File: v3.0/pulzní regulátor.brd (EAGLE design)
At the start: 27.9 x 53 mm, 18 parts, among them Q1 NX3008, Q2 NX3008, Q3 NX3008, Q4 NX3008

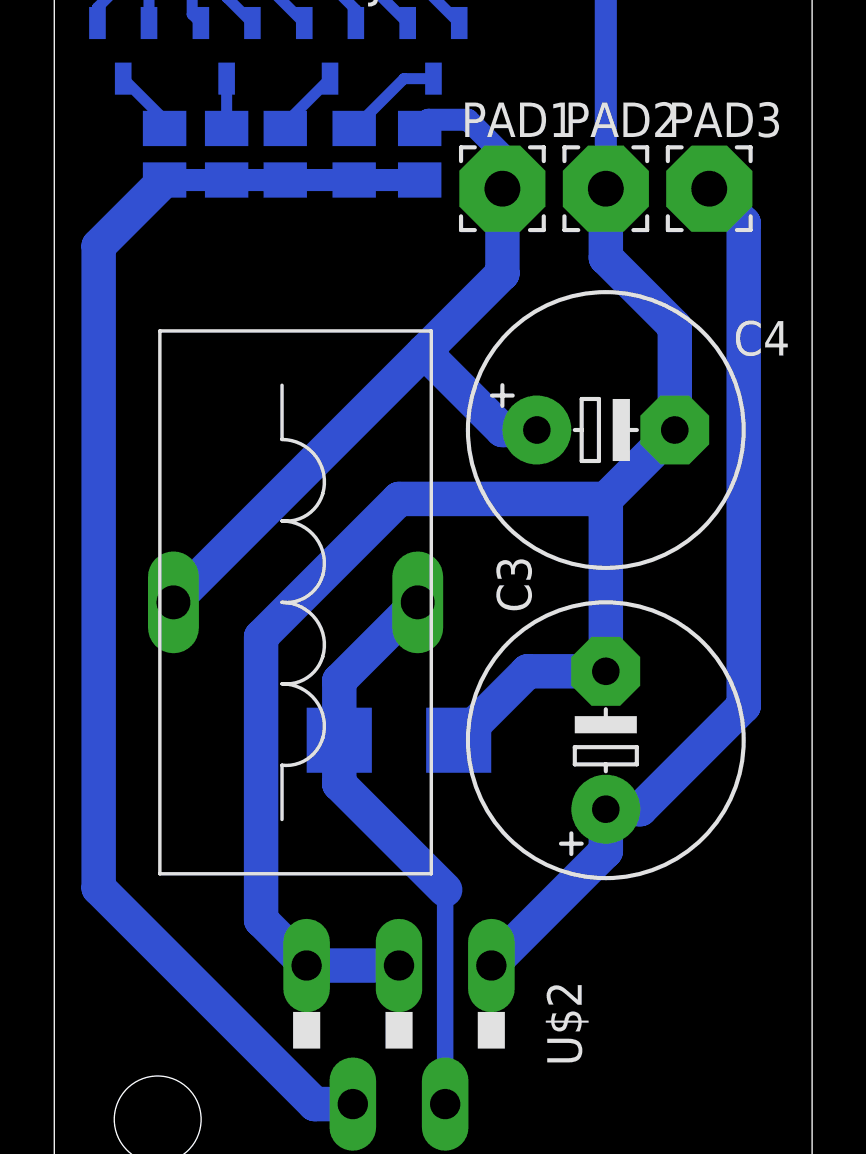
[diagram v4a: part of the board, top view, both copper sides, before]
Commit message: mírné úpravy dokumentace, přidání funkce pro zakázané stavy
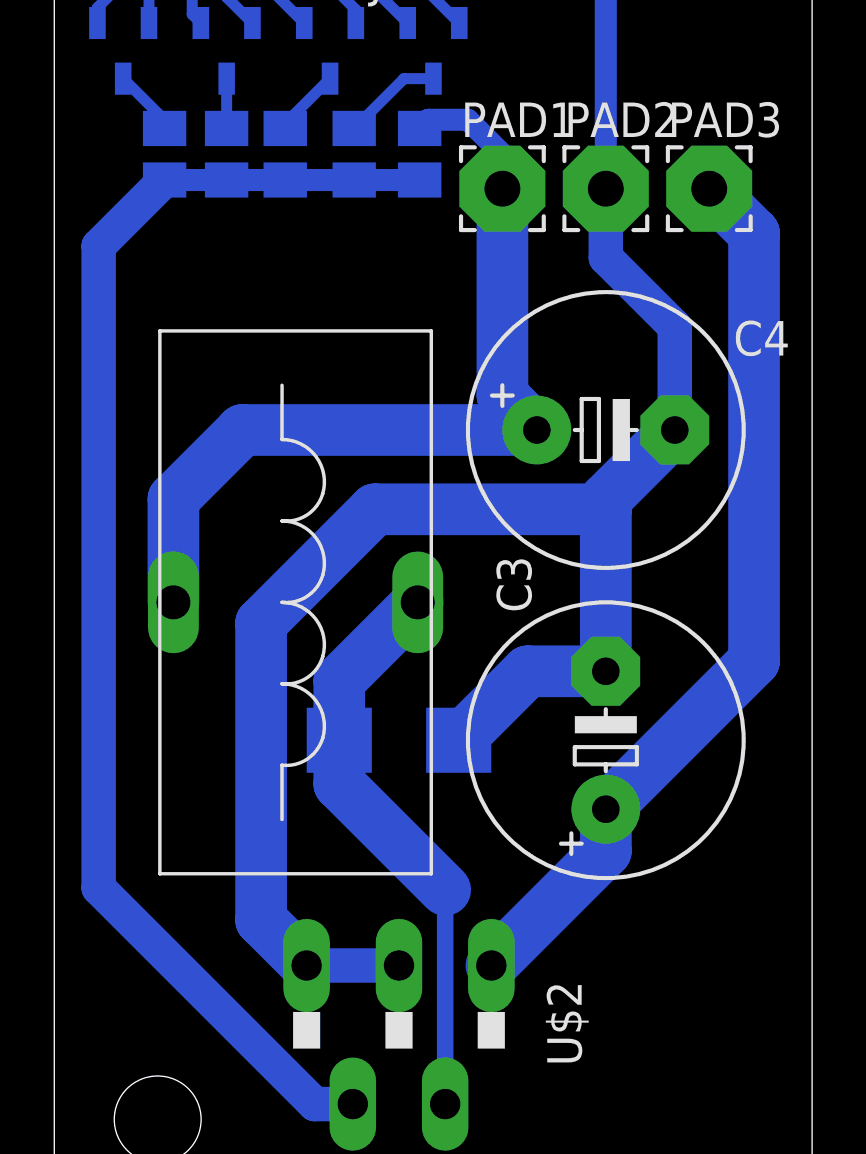
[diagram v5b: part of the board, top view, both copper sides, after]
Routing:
- net VCC: track 30.6 -> 32.6 mm
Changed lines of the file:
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@@
 <contactref element="C3" pad="+"/>
 <contactref element="PAD3" pad="1"/>
-<wire x1="16.1036" y1="9.4808" x2="20.32" y2="13.6972" width="1.27" layer="16"/>
-<wire x1="20.32" y1="13.6972" x2="20.32" y2="15.24" width="1.27" layer="16"/>
-<wire x1="24.13" y1="38.1" x2="25.4" y2="36.83" width="1.27" layer="16"/>
-<wire x1="25.4" y1="19.05" x2="21.59" y2="15.24" width="1.27" layer="16"/>
-<wire x1="21.59" y1="15.24" x2="20.32" y2="15.24" width="1.27" layer="16"/>
-<wire x1="25.4" y1="36.83" x2="25.4" y2="19.05" width="1.27" layer="16"/>
+<wire x1="16.1036" y1="9.4808" x2="20.32" y2="13.6972" width="1.905" layer="16"/>
+<wire x1="20.32" y1="13.6972" x2="20.32" y2="15.24" width="1.905" layer="16"/>
+<wire x1="20.32" y1="15.24" x2="25.781" y2="20.701" width="1.905" layer="16"/>
+<wire x1="25.781" y1="36.449" x2="25.781" y2="20.701" width="1.905" layer="16"/>
+<wire x1="24.13" y1="38.1" x2="25.781" y2="36.449" width="1.905" layer="16"/>
 </signal>
 <signal name="N$3">
@@
 <contactref element="U$2" pad="2"/>
 <contactref element="D2" pad="C"/>
-<wire x1="13.39" y1="22.86" x2="10.5" y2="19.97" width="1.27" layer="16"/>
-<wire x1="10.5" y1="19.97" x2="10.5" y2="17.78" width="1.27" layer="16"/>
 <wire x1="14.4018" y1="4.3754" x2="14.4018" y2="12.2682" width="0.6096" layer="16"/>
-<wire x1="10.5" y1="16.17" x2="10.5" y2="17.78" width="1.27" layer="16"/>
-<wire x1="14.4018" y1="12.2682" x2="10.5" y2="16.17" width="1.27" layer="16"/>
+<wire x1="10.5" y1="17.78" x2="10.5" y2="19.97" width="1.905" layer="16"/>
+<wire x1="10.5" y1="19.97" x2="13.39" y2="22.86" width="1.905" layer="16"/>
+<wire x1="10.5" y1="17.78" x2="10.5" y2="16.17" width="1.905" layer="16"/>
+<wire x1="10.5" y1="16.17" x2="14.4018" y2="12.2682" width="1.905" layer="16"/>
 </signal>
 <signal name="GND">
@@
 <wire x1="20.32" y1="38.1" x2="20.32" y2="45.72" width="0.8128" layer="16"/>
 <wire x1="20.32" y1="45.72" x2="17.78" y2="48.26" width="0.8128" layer="16"/>
-<wire x1="14.9" y1="17.78" x2="17.44" y2="20.32" width="1.27" layer="16"/>
-<wire x1="17.44" y1="20.32" x2="20.32" y2="20.32" width="1.27" layer="16"/>
 <wire x1="12.7" y1="9.4808" x2="9.2964" y2="9.4808" width="1.27" layer="16"/>
-<wire x1="9.2964" y1="9.4808" x2="7.62" y2="11.1572" width="1.27" layer="16"/>
-<wire x1="7.62" y1="21.59" x2="12.7" y2="26.67" width="1.27" layer="16"/>
-<wire x1="7.62" y1="11.1572" x2="7.62" y2="21.59" width="1.27" layer="16"/>
 <wire x1="20.32" y1="38.1" x2="20.32" y2="35.56" width="1.27" layer="16"/>
-<wire x1="12.7" y1="26.67" x2="20.32" y2="26.67" width="1.27" layer="16"/>
-<wire x1="20.32" y1="26.67" x2="22.86" y2="29.21" width="1.27" layer="16"/>
 <wire x1="11.43" y1="50.8" x2="12.7" y2="49.53" width="0.8128" layer="16"/>
 <wire x1="6.35" y1="50.8" x2="4.445" y2="50.8" width="0.8128" layer="16"/>
 <wire x1="3.81" y1="50.165" x2="4.445" y2="50.8" width="0.4064" layer="16"/>
-<wire x1="20.32" y1="20.32" x2="20.32" y2="26.67" width="1.27" layer="16"/>
 <wire x1="20.32" y1="35.56" x2="22.86" y2="33.02" width="1.27" layer="16"/>
 <wire x1="22.86" y1="33.02" x2="22.86" y2="29.21" width="1.27" layer="16"/>
+<wire x1="9.2964" y1="9.4808" x2="7.62" y2="11.1572" width="1.905" layer="16"/>
+<wire x1="7.62" y1="11.1572" x2="7.62" y2="22.098" width="1.905" layer="16"/>
+<wire x1="7.62" y1="22.098" x2="11.811" y2="26.289" width="1.905" layer="16"/>
+<wire x1="20.32" y1="26.289" x2="11.811" y2="26.289" width="1.905" layer="16"/>
+<wire x1="22.86" y1="29.21" x2="20.32" y2="26.67" width="1.905" layer="16"/>
+<wire x1="20.32" y1="20.32" x2="20.32" y2="26.289" width="1.905" layer="16"/>
+<wire x1="20.32" y1="26.289" x2="20.32" y2="26.67" width="1.905" layer="16"/>
+<wire x1="14.9" y1="17.78" x2="17.44" y2="20.32" width="1.905" layer="16"/>
+<wire x1="17.44" y1="20.32" x2="20.32" y2="20.32" width="1.905" layer="16"/>
 </signal>
 <signal name="N$6">
@@
 <wire x1="15.24" y1="40.64" x2="16.51" y2="39.37" width="0.8128" layer="16"/>
 <wire x1="16.51" y1="39.37" x2="16.51" y2="38.1" width="0.8128" layer="16"/>
-<wire x1="16.51" y1="34.98" x2="16.51" y2="38.1" width="1.27" layer="16"/>
-<wire x1="4.39" y1="22.86" x2="13.625" y2="32.095" width="1.27" layer="16"/>
-<wire x1="13.625" y1="32.095" x2="16.51" y2="34.98" width="1.27" layer="16"/>
-<wire x1="17.78" y1="29.21" x2="16.51" y2="29.21" width="1.27" layer="16"/>
-<wire x1="16.51" y1="29.21" x2="13.625" y2="32.095" width="1.27" layer="16"/>
+<wire x1="6.93" y1="29.21" x2="4.39" y2="26.67" width="1.905" layer="16"/>
+<wire x1="4.39" y1="22.86" x2="4.39" y2="26.67" width="1.905" layer="16"/>
+<wire x1="6.93" y1="29.21" x2="17.78" y2="29.21" width="1.905" layer="16"/>
+<wire x1="17.78" y1="29.21" x2="16.51" y2="30.48" width="1.905" layer="16"/>
+<wire x1="16.51" y1="30.48" x2="16.51" y2="38.1" width="1.905" layer="16"/>
 </signal>
 </signals>

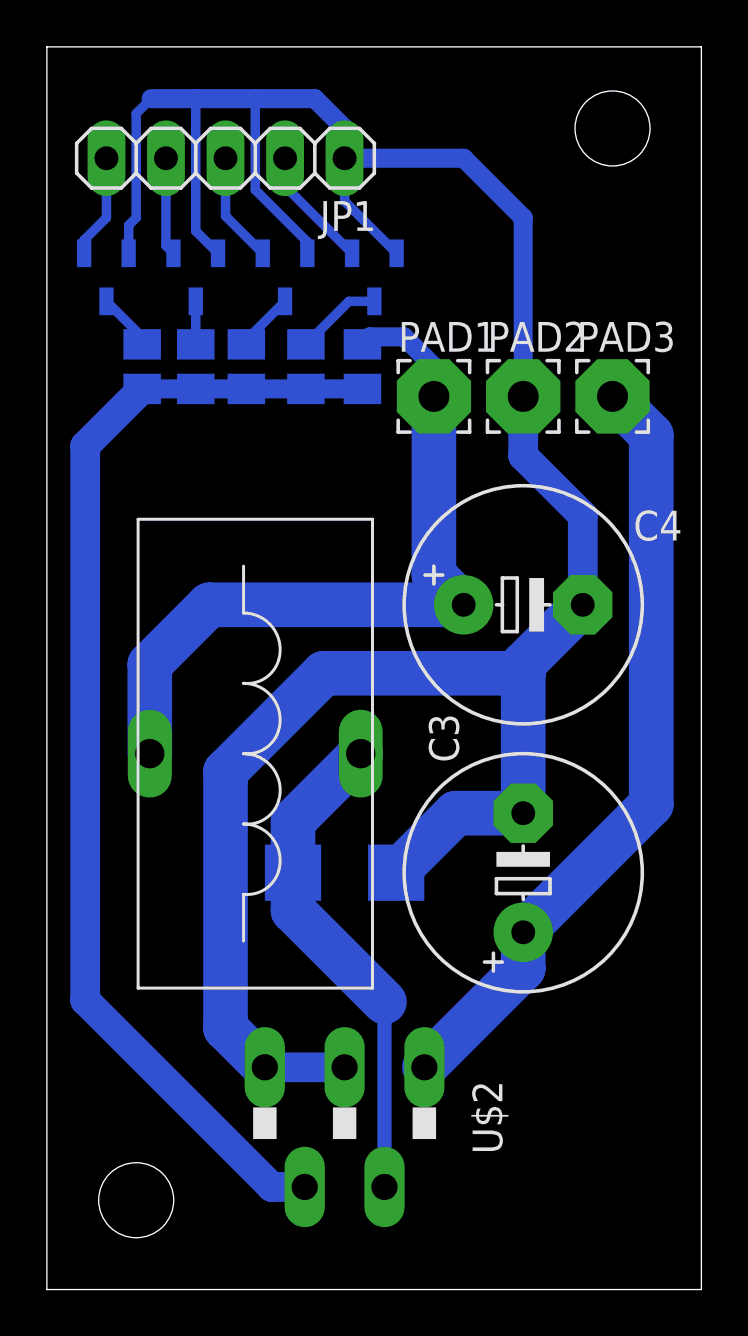
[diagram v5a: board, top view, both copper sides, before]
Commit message: přidána rozlévaná měď, rozšířena dokumentace
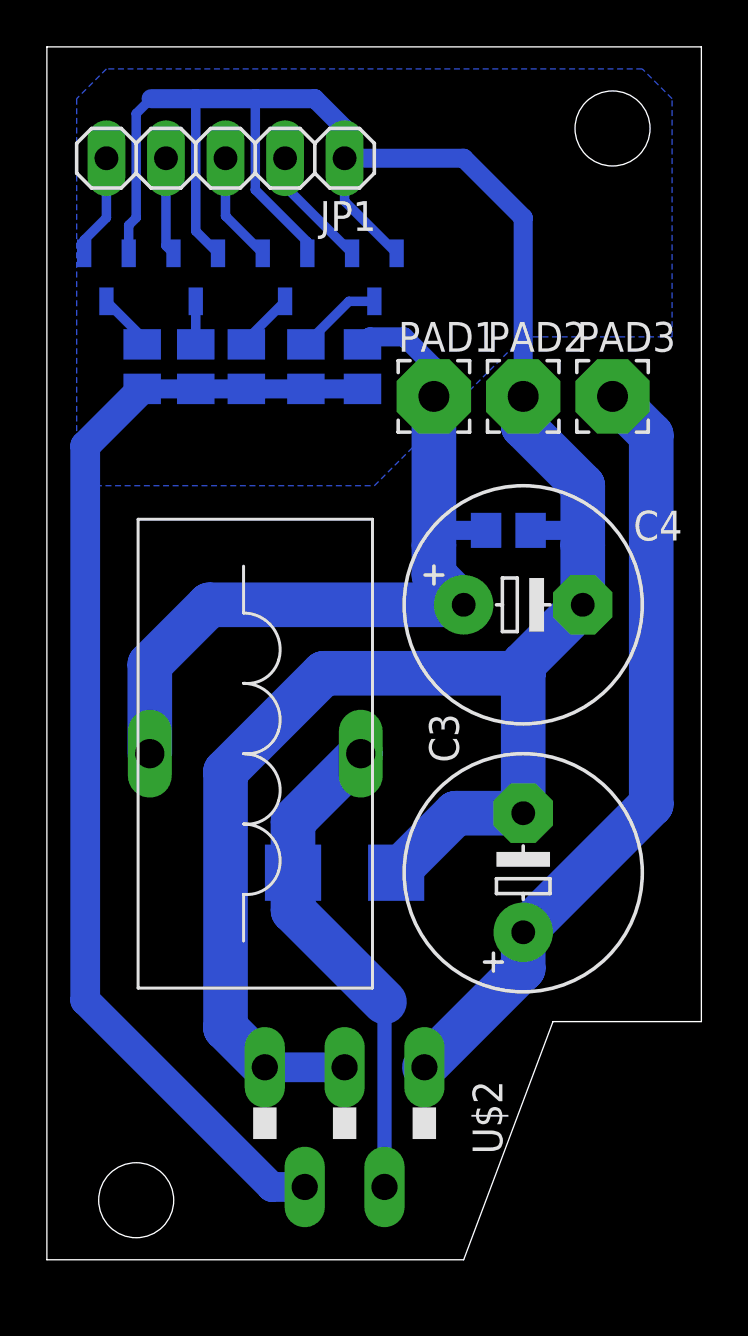
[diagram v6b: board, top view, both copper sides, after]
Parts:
- added R6: (no value), rcl:R0805
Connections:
- net GND: now also R6.1
- net VCC: now also R6.2
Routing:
- net VCC: track 32.6 -> 35.1 mm
- net GND: track 110.3 -> 112.8 mm
- added copper zone on layer 16, net GND
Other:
- board size 27.9 x 53 mm -> 27.9 x 51.7 mm
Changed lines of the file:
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@@
 </layers>
 <board>
-<fusionsync huburn="a.YnVzaW5lc3M6c3BzdHJ1dG5vdjM" projecturn="a.YnVzaW5lc3M6c3BzdHJ1dG5vdjMjMjAyMDAzMzEyODExMTAyMDY" f3durn="urn:adsk.wipprod:dm.lineage:Wyhkb4j1T3y43OJJPs_q7g" pcbguid="c6696d83-4a0f-42e7-b2fc-2a2a6b268699" lastpulledtime="" lastsyncedchangeguid="b4cc55c6-0a59-03e3-4777-97c5f8477c91"/>
+<fusionsync huburn="a.YnVzaW5lc3M6c3BzdHJ1dG5vdjM" projecturn="a.YnVzaW5lc3M6c3BzdHJ1dG5vdjMjMjAyMDAzMzEyODExMTAyMDY" f3durn="urn:adsk.wipprod:dm.lineage:Wyhkb4j1T3y43OJJPs_q7g" pcbguid="c6696d83-4a0f-42e7-b2fc-2a2a6b268699" lastpulledtime="" lastsyncedchangeguid="5f48968b-f0e6-1f98-428d-cf6b1e6b6569"/>
 <plain>
-<wire x1="0" y1="0" x2="27.92" y2="0" width="0" layer="20"/>
-<wire x1="27.92" y1="0" x2="27.92" y2="53.01" width="0" layer="20"/>
+<wire x1="0" y1="1.27" x2="17.78" y2="1.27" width="0" layer="20"/>
+<wire x1="17.78" y1="1.27" x2="21.59" y2="11.43" width="0" layer="20"/>
+<wire x1="21.59" y1="11.43" x2="27.92" y2="11.43" width="0" layer="20"/>
+<wire x1="27.92" y1="11.43" x2="27.92" y2="53.01" width="0" layer="20"/>
 <wire x1="27.92" y1="53.01" x2="0" y2="53.01" width="0" layer="20"/>
-<wire x1="0" y1="53.01" x2="0" y2="0" width="0" layer="20"/>
+<wire x1="0" y1="53.01" x2="0" y2="1.27" width="0" layer="20"/>
 <hole x="3.81" y="3.81" drill="3.2"/>
 <hole x="24.13" y="49.53" drill="3.2"/>
@@
 </element>
 <element name="U$4" library="induktory a trafa" package="DTMSS-16/0,033/6,0" package3d_urn="urn:adsk.eagle:package:24991841/2" value="DTMSSDTMSS-16/0,033/6,0" x="8.89" y="22.86" smashed="yes" rot="R270"/>
+<element name="R6" library="rcl" library_urn="urn:adsk.eagle:library:334" package="R0805" package3d_urn="urn:adsk.eagle:package:23553/2" value="" x="19.685" y="32.385" smashed="yes" rot="MR0">
+<attribute name="NAME" x="20.32" y="33.655" size="1.27" layer="26" rot="MR0"/>
+<attribute name="POPULARITY" value="86" x="19.685" y="32.385" size="1.778" layer="28" rot="MR0" display="off"/>
+<attribute name="SPICEPREFIX" value="R" x="19.685" y="32.385" size="1.778" layer="28" rot="MR0" display="off"/>
+<attribute name="VALUE" x="20.32" y="29.845" size="1.27" layer="28" rot="MR0"/>
+</element>
 </elements>
 <signals>
@@
 <wire x1="20.32" y1="45.72" x2="17.78" y2="48.26" width="0.8128" layer="16"/>
 <wire x1="12.7" y1="9.4808" x2="9.2964" y2="9.4808" width="1.27" layer="16"/>
-<wire x1="20.32" y1="38.1" x2="20.32" y2="35.56" width="1.27" layer="16"/>
 <wire x1="11.43" y1="50.8" x2="12.7" y2="49.53" width="0.8128" layer="16"/>
 <wire x1="6.35" y1="50.8" x2="4.445" y2="50.8" width="0.8128" layer="16"/>
 <wire x1="3.81" y1="50.165" x2="4.445" y2="50.8" width="0.4064" layer="16"/>
-<wire x1="20.32" y1="35.56" x2="22.86" y2="33.02" width="1.27" layer="16"/>
-<wire x1="22.86" y1="33.02" x2="22.86" y2="29.21" width="1.27" layer="16"/>
 <wire x1="9.2964" y1="9.4808" x2="7.62" y2="11.1572" width="1.905" layer="16"/>
 <wire x1="7.62" y1="11.1572" x2="7.62" y2="22.098" width="1.905" layer="16"/>
@@
 <wire x1="14.9" y1="17.78" x2="17.44" y2="20.32" width="1.905" layer="16"/>
 <wire x1="17.44" y1="20.32" x2="20.32" y2="20.32" width="1.905" layer="16"/>
+<contactref element="R6" pad="1"/>
+<wire x1="20.635" y1="32.385" x2="22.225" y2="32.385" width="0.8128" layer="16"/>
+<wire x1="22.225" y1="32.385" x2="22.86" y2="31.75" width="0.8128" layer="16"/>
+<wire x1="22.86" y1="29.21" x2="22.86" y2="31.75" width="1.905" layer="16"/>
+<wire x1="22.86" y1="31.75" x2="22.86" y2="34.29" width="1.905" layer="16"/>
+<wire x1="22.86" y1="34.29" x2="20.32" y2="36.83" width="1.905" layer="16"/>
+<wire x1="20.32" y1="38.1" x2="20.32" y2="36.83" width="1.905" layer="16"/>
+<polygon width="0.254" layer="16" isolate="0.4064">
+<vertex x="1.27" y="34.29"/>
+<vertex x="13.97" y="34.29"/>
+<vertex x="20.32" y="40.64"/>
+<vertex x="26.67" y="40.64"/>
+<vertex x="26.67" y="50.8"/>
+<vertex x="25.4" y="52.07"/>
+<vertex x="2.54" y="52.07"/>
+<vertex x="1.27" y="50.8"/>
+</polygon>
 </signal>
 <signal name="N$6">
@@
 <wire x1="6.93" y1="29.21" x2="17.78" y2="29.21" width="1.905" layer="16"/>
 <wire x1="17.78" y1="29.21" x2="16.51" y2="30.48" width="1.905" layer="16"/>
-<wire x1="16.51" y1="30.48" x2="16.51" y2="38.1" width="1.905" layer="16"/>
+<wire x1="16.51" y1="30.48" x2="16.51" y2="31.75" width="1.905" layer="16"/>
+<contactref element="R6" pad="2"/>
+<wire x1="16.51" y1="31.75" x2="16.51" y2="38.1" width="1.905" layer="16"/>
+<wire x1="18.735" y1="32.385" x2="17.145" y2="32.385" width="0.8128" layer="16"/>
+<wire x1="17.145" y1="32.385" x2="16.51" y2="31.75" width="0.8128" layer="16"/>
 </signal>
 </signals>
